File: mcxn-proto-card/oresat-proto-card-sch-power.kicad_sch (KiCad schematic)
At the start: 87 parts, among them Q1 DMP2240UDM, Q2 DMP3050LVT-7, Q7 DMP3050LVT-7, Q8 PMV45EN, Q9 PMV45EN, U10 TPS62111RSA, U11 MIC842LYC5, U12 MIC842LYC5, U2 MAX7310, U3 TS5A21366DCUR, U6 MAX4211FETE

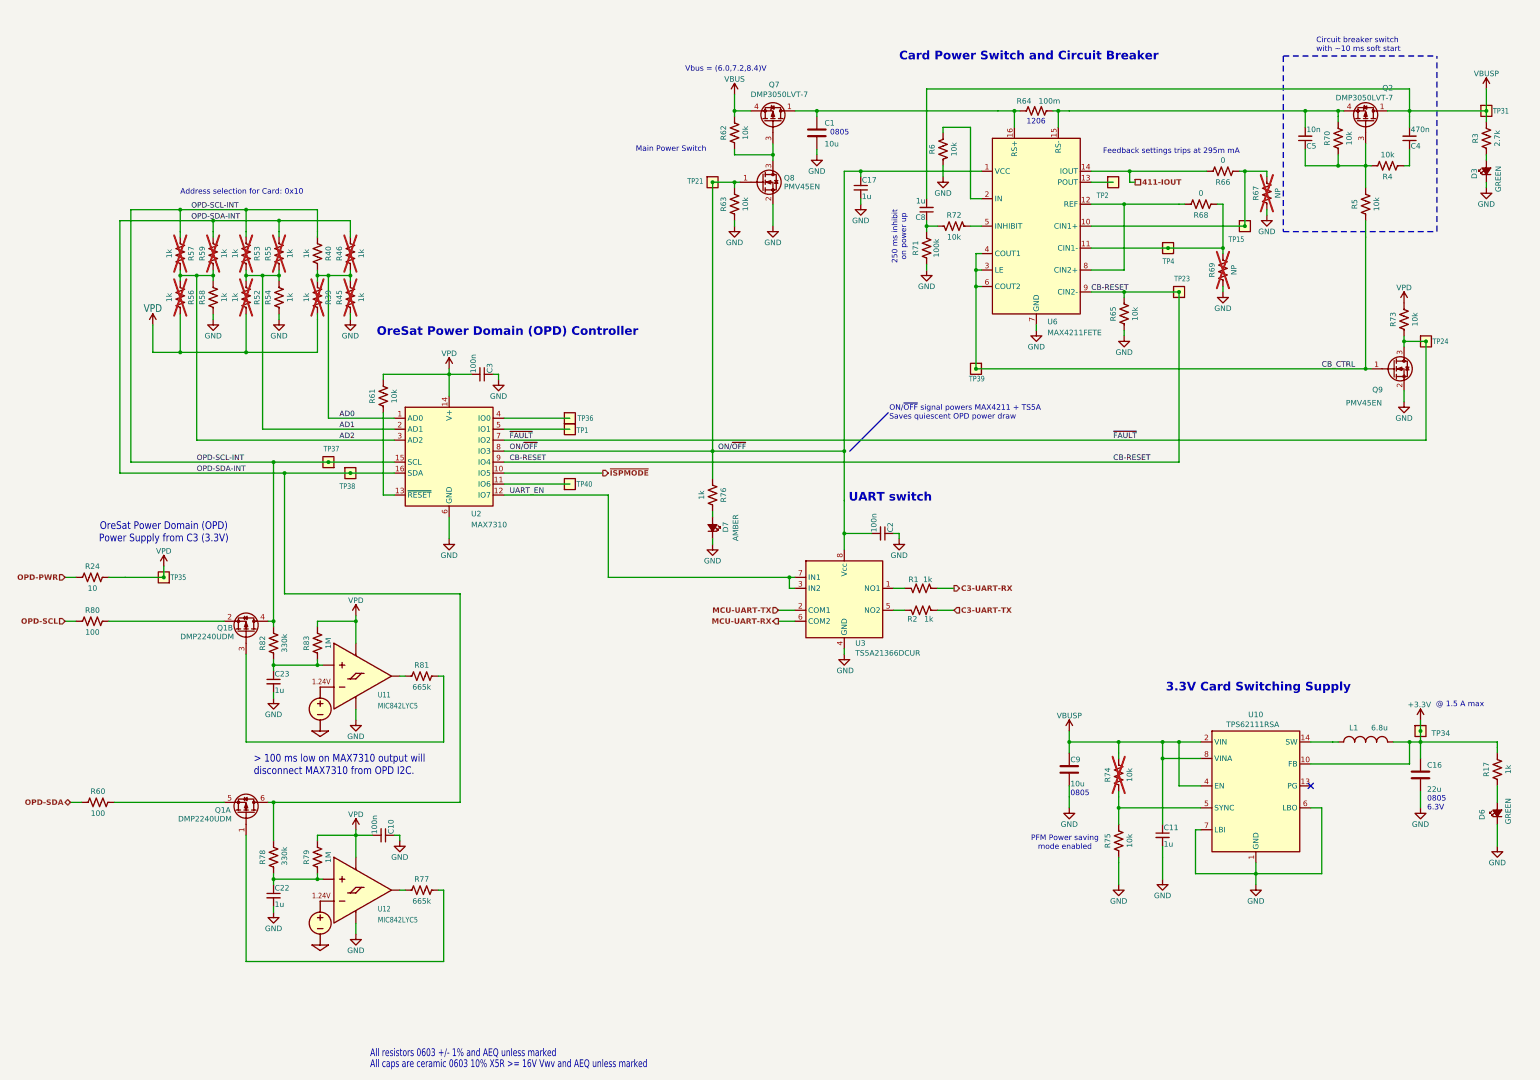
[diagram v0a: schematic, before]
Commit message: Update protocard
Update to 10.0.4, new .gitignore, better hierachical layout, updated footprints, re-arranged LEDs, brought outline and SMPMs into latest standards, all but OPD is updated.
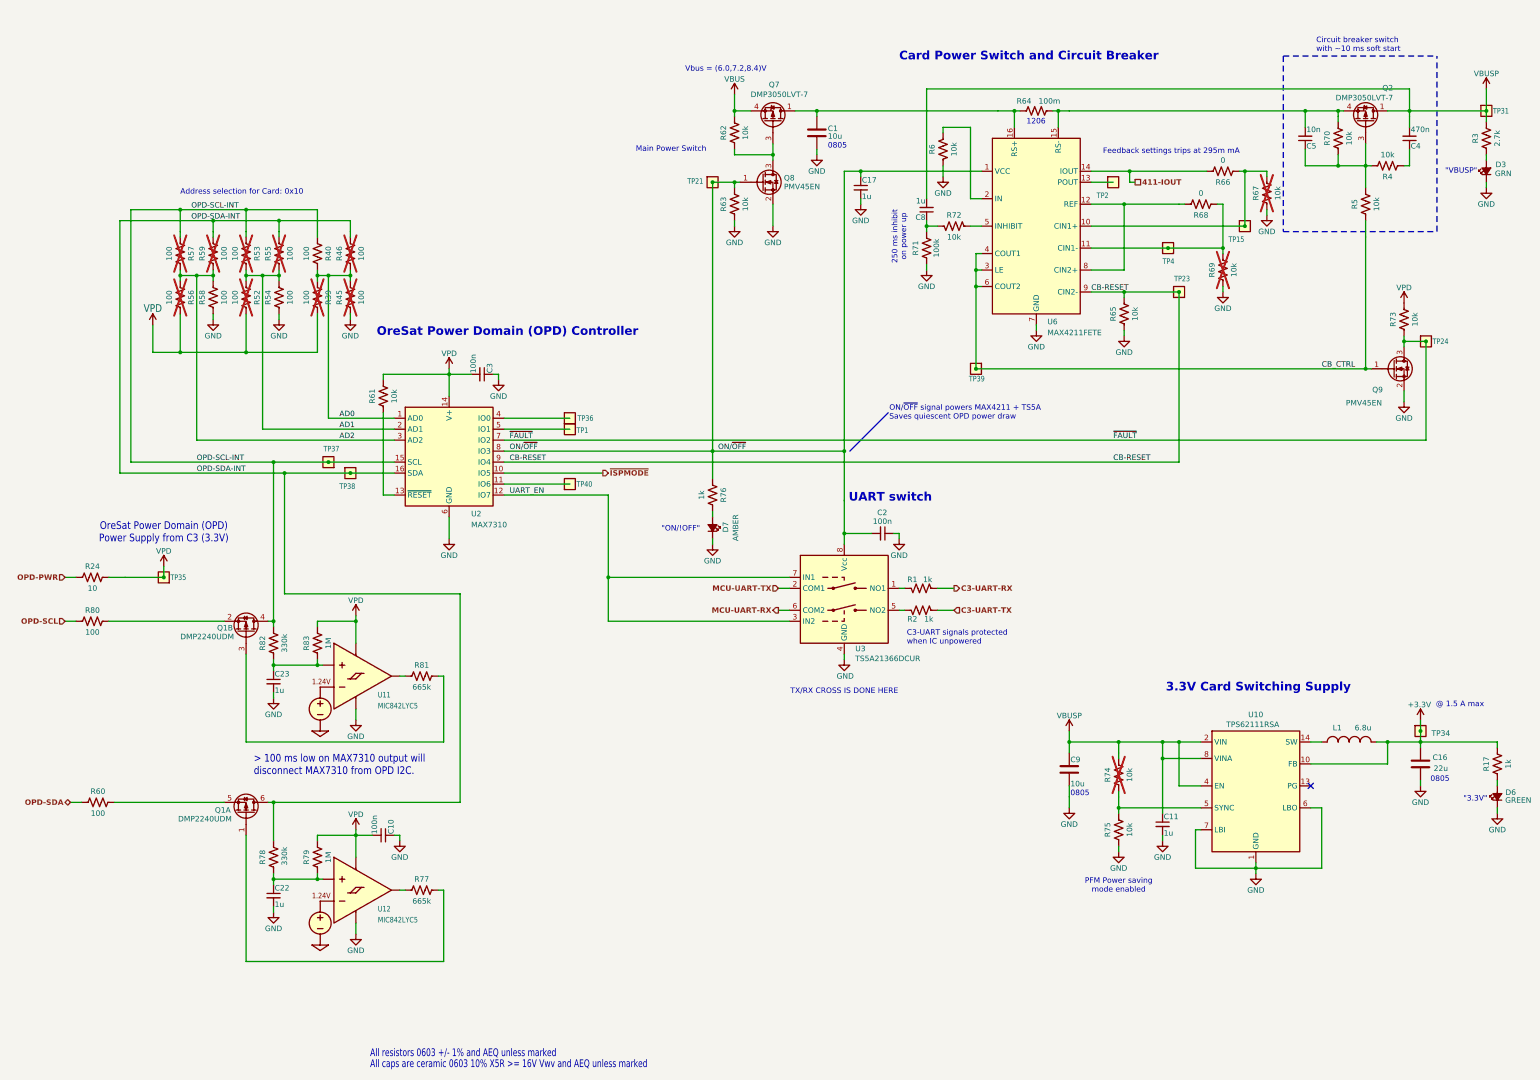
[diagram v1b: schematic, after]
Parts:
- C16: footprint oresat-passives:0805-B-NOSILK -> oresat-passives:0805-C-NOSILK; DPN 478-KAM21AT70J226KUCT-ND -> 490-GRT21BC81C226ME13LCT-ND; MFR KYOCERA AVX -> Murata Electronics; MPN KAM21AT70J226KU -> GRT21BC81C226ME13L
- D3: value GREEN -> GRN
- R39, R45, R46, R52, R53, R55, R56, R57, R59: value 1k -> 100; DIS Digi-Key -> DigiKey; DPN 1276-4275-1-ND -> RMCF0603FT100RCT-ND; MFR Samsung -> Stackpole Electronics Inc; MPN RC1005F6653CS -> RMCF0603FT100R
- R40, R54, R58: value 1k -> 100; DPN RMCF0603FT1K00CT-ND -> RMCF0603FT100RCT-ND; MPN RMCF0603FT1K00 -> RMCF0603FT100R
- R67, R69: value NP -> 10k; DIS Digi-Key -> DigiKey; DPN 1276-4275-1-ND -> RMCF0603FT10K0CT-ND; MFR Samsung -> Stackpole Electronics Inc; MPN RC1005F6653CS -> RMCF0603FT10K0
- R74: DIS Digi-Key -> DigiKey; DPN RNCP0603FTD10K0CT-ND -> RMCF0603FT10K0CT-ND; MFR Stackpole -> Stackpole Electronics Inc; MPN RNCP0603FTD10K0 -> RMCF0603FT10K0
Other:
- note added: ""3.3V""
- note added: ""ON/!OFF""
- note added: ""VBUSP""
- note added: "C3-UART signals protected when IC unpowered"
- note added: "TX/RX CROSS IS DONE HERE"
- note removed: "0805 6.3V"
- moved on the sheet: C11, C16, D6, L1, R17, R75

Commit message: Small cleanups for manufacturing
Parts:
- Q1: value DMP2240UDM -> DMP2110UVTQ-7; DPN DMP2240UDMDICT-ND -> 31-DMP2110UVTQ-7CT-ND; MFR Diodes Inc -> Diodes Incorporated; MPN DMP2240UDM -> DMP2110UVTQ-7
- Q2, Q7: value DMP3050LVT-7 -> DMPH2040UVTQ-7; DPN DMP3050LVT-7DICT-ND -> 31-DMPH2040UVTQ-7CT-ND; MFR Diodes Inc -> Diodes Incorporated; MPN DMP3050LVT-7 -> DMPH2040UVTQ-7
- Q8, Q9: value PMV45EN -> DMN2050LQ-7; DPN 1727-2307-1-ND -> 31-DMN2050LQ-7CT-ND; MFR Nexperia -> Diodes Incorporated; MPN PMV45EN2R -> DMN2050LQ-7
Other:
- note added: "AUTOMOTIVE GRADE IC?"
- note added: "OH WAIT - ON TURN ON, Q2 PROBABLY DOESN'T SOFT START!!!"
- moved on the sheet: R5
